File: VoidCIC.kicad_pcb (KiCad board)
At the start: 2 copper layers, 11.5 x 23 mm, 8 parts, among them U1 SN74LVC1GU04DBVR

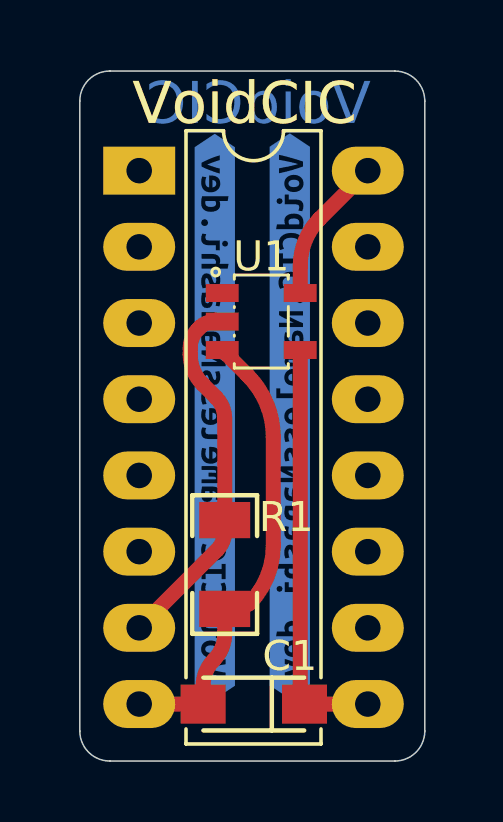
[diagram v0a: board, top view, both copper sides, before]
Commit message: Increase hole size more and round board to make the fixed version more apparent and hopefully make it look better
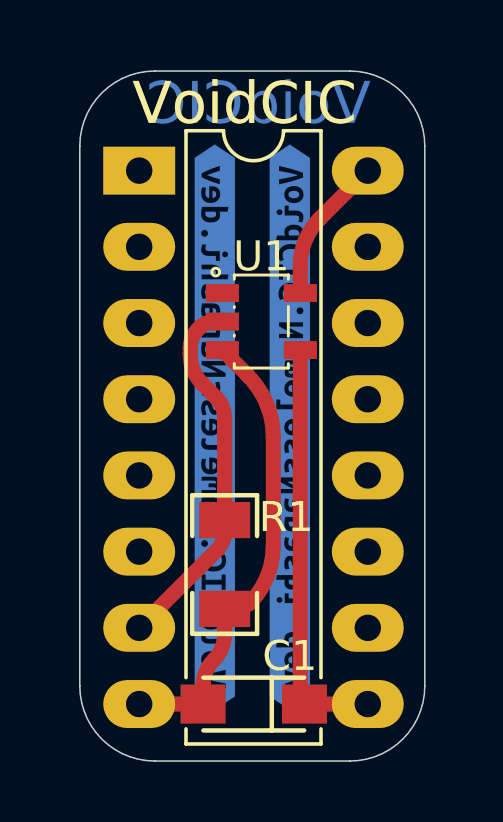
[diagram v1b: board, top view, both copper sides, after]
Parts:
- moved kibuzzard-675A635B 0.37 mm to (152.1, 98.2)
- moved kibuzzard-675A6399 0.37 mm to (152.1, 98.2)
- moved kibuzzard-675A635B 0.36 mm to (149.6, 98.2)
- moved kibuzzard-675A6399 0.36 mm to (149.6, 98.2)
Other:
- outline, holes or cut-outs redrawn
